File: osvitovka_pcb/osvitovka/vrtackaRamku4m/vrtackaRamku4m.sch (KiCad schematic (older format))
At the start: 21 parts, among them J1 Screw_Terminal_01x01, J2 Screw_Terminal_01x01, J3 M+, J4 M-, K1 RSM822, Q1 BC817, U1 LM78M05_TO220

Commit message: test a upgrade pcb.
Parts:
- D1, D2: footprint Diode_SMD:D_1206_3216Metric -> Diode_SMD:D_1806_4516Metric_Pad1.57x1.80mm_HandSolder
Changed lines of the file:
@@
 F 0 "D2" V 6554 3279 50  0000 L CNN
 F 1 "D" V 6645 3279 50  0000 L CNN
-F 2 "Diode_SMD:D_1206_3216Metric" H 6600 3200 50  0001 C CNN
+F 2 "Diode_SMD:D_1806_4516Metric_Pad1.57x1.80mm_HandSolder" H 6600 3200 50  0001 C CNN
 F 3 "~" H 6600 3200 50  0001 C CNN
 	1    6600 3200
@@
 F 0 "D1" H 5300 2666 50  0000 C CNN
 F 1 "D" H 5300 2575 50  0000 C CNN
-F 2 "Diode_SMD:D_1206_3216Metric" H 5300 2450 50  0001 C CNN
+F 2 "Diode_SMD:D_1806_4516Metric_Pad1.57x1.80mm_HandSolder" H 5300 2450 50  0001 C CNN
 F 3 "~" H 5300 2450 50  0001 C CNN
 	1    5300 2450

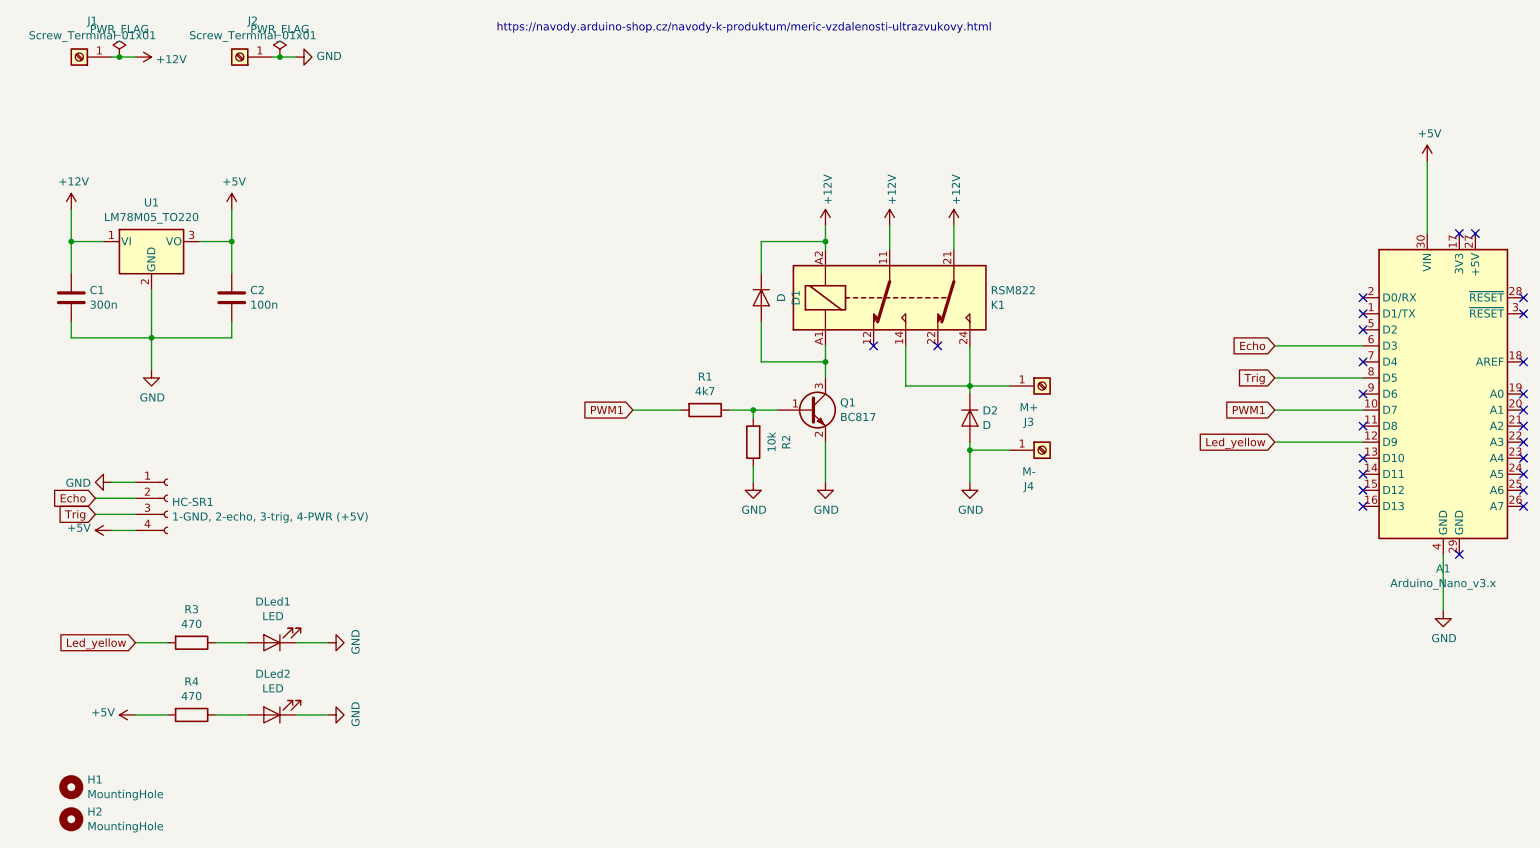
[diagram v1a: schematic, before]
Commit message: Totálně předělaný plošňák. Zvětšené plošky, širší cestičky. Založena vlastní knihovna.
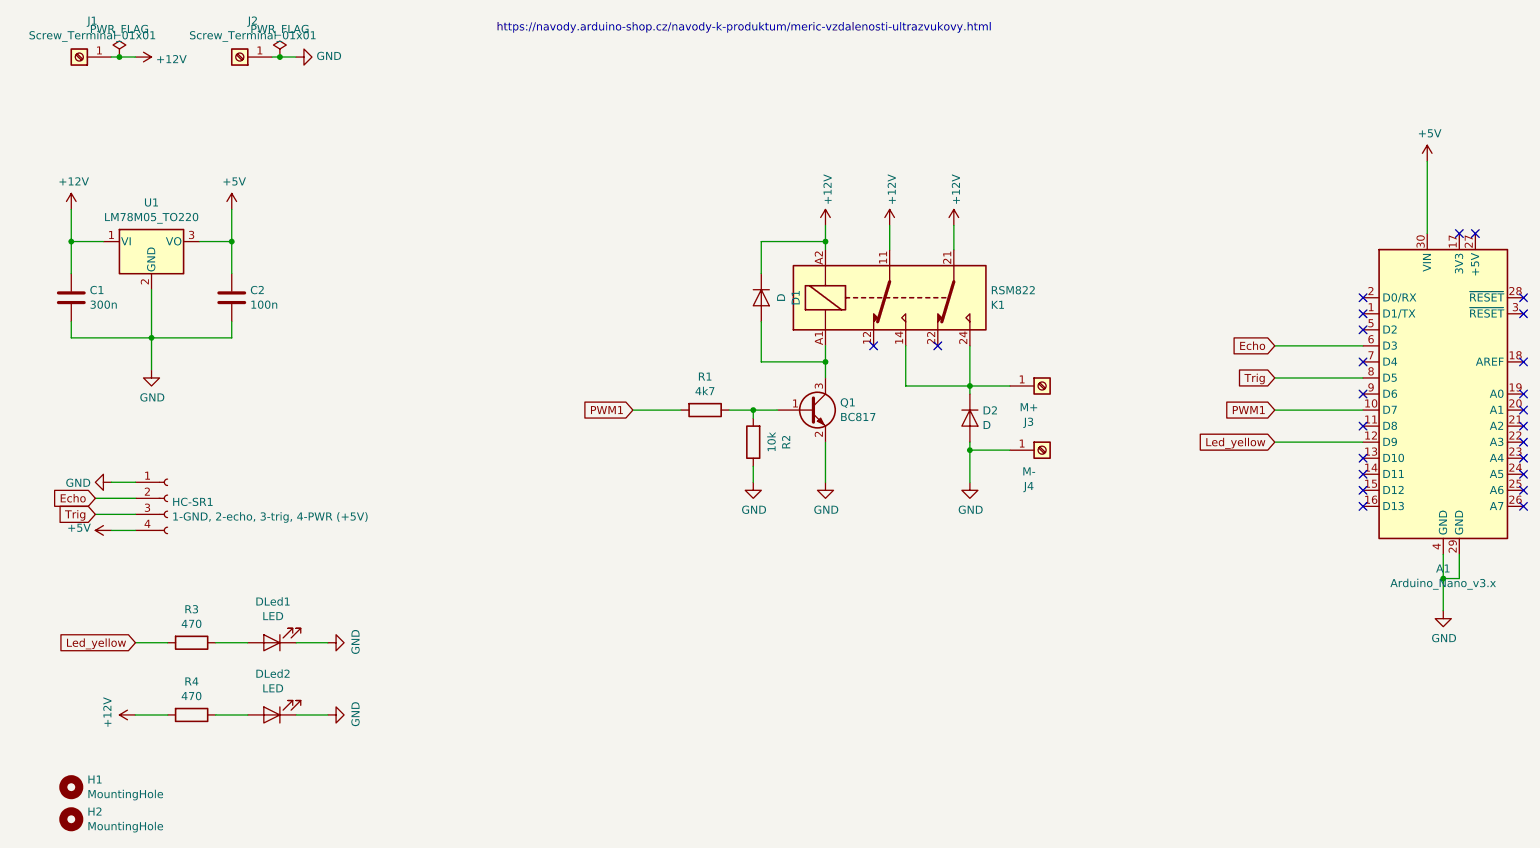
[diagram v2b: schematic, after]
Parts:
- A1: footprint Module:Arduino_Nano -> LPouzdra:Arduino_Nano_vetsi_plosky
- C1, C2: footprint Capacitor_THT:C_Disc_D3.0mm_W2.0mm_P2.50mm -> LPouzdra:AR_C_Disc_D3.0mm_W2.0mm_P2.50mm
- D1, D2: footprint Diode_SMD:D_1806_4516Metric_Pad1.57x1.80mm_HandSolder -> Diode_SMD:D_2010_5025Metric_Pad1.52x2.65mm_HandSolder
- DLed1, DLed2: footprint LED_THT:LED_D3.0mm -> LPouzdra:AR_LED_D3.0mm
- HC-SR1: footprint Connector_PinHeader_2.54mm:PinHeader_1x04_P2.54mm_Vertical -> LPouzdra:AR_PinHeader_1x04_P2.54mm_Vertical
- K1: footprint Relay_THT:Relay_DPDT_Finder_30.22 -> LPouzdra:AR_Relay_DPDT_Finder_30.22
- U1: footprint Package_TO_SOT_THT:TO-220-3_Vertical -> LPouzdra:AR_TO-220-3_Vertical
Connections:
- net +12V: now also R4.2
- net +5V: no longer R4.2
- net GND: now also A1.29 (GND)
- no-connect marks 26 -> 25
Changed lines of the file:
@@
 F 0 "C1" H 1115 2496 50  0000 L CNN
 F 1 "300n" H 1115 2405 50  0000 L CNN
-F 2 "Capacitor_THT:C_Disc_D3.0mm_W2.0mm_P2.50mm" H 1038 2300 50  0001 C CNN
+F 2 "LPouzdra:AR_C_Disc_D3.0mm_W2.0mm_P2.50mm" H 1038 2300 50  0001 C CNN
 F 3 "~" H 1000 2450 50  0001 C CNN
 	1    1000 2450
@@
 F 0 "U1" H 1500 2342 50  0000 C CNN
 F 1 "LM78M05_TO220" H 1500 2251 50  0000 C CNN
-F 2 "Package_TO_SOT_THT:TO-220-3_Vertical" H 1500 2325 50  0001 C CIN
+F 2 "LPouzdra:AR_TO-220-3_Vertical" H 1500 2325 50  0001 C CIN
 F 3 "http://www.fairchildsemi.com/ds/LM/LM78M05.pdf" H 1500 2050 50  0001 C CNN
 	1    1500 2100
@@
 F 0 "C2" H 2115 2496 50  0000 L CNN
 F 1 "100n" H 2115 2405 50  0000 L CNN
-F 2 "Capacitor_THT:C_Disc_D3.0mm_W2.0mm_P2.50mm" H 2038 2300 50  0001 C CNN
+F 2 "LPouzdra:AR_C_Disc_D3.0mm_W2.0mm_P2.50mm" H 2038 2300 50  0001 C CNN
 F 3 "~" H 2000 2450 50  0001 C CNN
 	1    2000 2450
@@
 F 0 "HC-SR1" H 1628 3676 50  0000 L CNN
 F 1 "1-GND, 2-echo, 3-trig, 4-PWR (+5V)" H 1628 3585 50  0000 L CNN
-F 2 "Connector_PinHeader_2.54mm:PinHeader_1x04_P2.54mm_Vertical" H 1600 3700 50  0001 C CNN
+F 2 "LPouzdra:AR_PinHeader_1x04_P2.54mm_Vertical" H 1600 3700 50  0001 C CNN
 F 3 "~" H 1600 3700 50  0001 C CNN
 	1    1600 3700
@@
 F 0 "DLed1" H 2243 4345 50  0000 C CNN
 F 1 "LED" H 2243 4436 50  0000 C CNN
-F 2 "LED_THT:LED_D3.0mm" H 2250 4600 50  0001 C CNN
+F 2 "LPouzdra:AR_LED_D3.0mm" H 2250 4600 50  0001 C CNN
 F 3 "~" H 2250 4600 50  0001 C CNN
 	1    2250 4600
@@
 F 0 "DLed2" H 2243 4795 50  0000 C CNN
 F 1 "LED" H 2243 4886 50  0000 C CNN
-F 2 "LED_THT:LED_D3.0mm" H 2250 5050 50  0001 C CNN
+F 2 "LPouzdra:AR_LED_D3.0mm" H 2250 5050 50  0001 C CNN
 F 3 "~" H 2250 5050 50  0001 C CNN
 	1    2250 5050
@@
 F 0 "A1" H 9550 1961 50  0000 C CNN
 F 1 "Arduino_Nano_v3.x" H 9550 1870 50  0000 C CNN
-F 2 "Module:Arduino_Nano" H 9550 3050 50  0001 C CIN
+F 2 "LPouzdra:Arduino_Nano_vetsi_plosky" H 9550 3050 50  0001 C CIN
 F 3 "http://www.mouser.com/pdfdocs/Gravitech_Arduino_Nano3_0.pdf" H 9550 3050 50  0001 C CNN
 	1    9550 3050
@@
 	8500 3350 9050 3350
 Wire Wire Line
-	9550 4050 9550 4400
+	9550 4050 9550 4200
 Wire Wire Line
 	9450 1600 9450 2050
@@
 	8500 2950 9050 2950
 NoConn ~ 9050 2850
-NoConn ~ 9650 4050
 Wire Wire Line
 	8500 3150 9050 3150
@@
 F 0 "K1" H 6730 2496 50  0000 L CNN
 F 1 "RSM822" H 6730 2405 50  0000 L CNN
-F 2 "Relay_THT:Relay_DPDT_Finder_30.22" H 7450 2420 50  0001 C CNN
+F 2 "LPouzdra:AR_Relay_DPDT_Finder_30.22" H 7450 2420 50  0001 C CNN
 F 3 "http://www.relpol.pl/en/content/download/14975/202519/file/e_RSM822.pdf" H 6100 2450 50  0001 C CNN
 	1    6100 2450
@@
 F 0 "D2" V 6554 3279 50  0000 L CNN
 F 1 "D" V 6645 3279 50  0000 L CNN
-F 2 "Diode_SMD:D_1806_4516Metric_Pad1.57x1.80mm_HandSolder" H 6600 3200 50  0001 C CNN
+F 2 "Diode_SMD:D_2010_5025Metric_Pad1.52x2.65mm_HandSolder" H 6600 3200 50  0001 C CNN
 F 3 "~" H 6600 3200 50  0001 C CNN
 	1    6600 3200
@@
 F 0 "D1" H 5300 2666 50  0000 C CNN
 F 1 "D" H 5300 2575 50  0000 C CNN
-F 2 "Diode_SMD:D_1806_4516Metric_Pad1.57x1.80mm_HandSolder" H 5300 2450 50  0001 C CNN
+F 2 "Diode_SMD:D_2010_5025Metric_Pad1.52x2.65mm_HandSolder" H 5300 2450 50  0001 C CNN
 F 3 "~" H 5300 2450 50  0001 C CNN
 	1    5300 2450
@@
 Wire Wire Line
 	6600 3050 6600 3000
-$Comp
-L power:+5V #PWR0101
-U 1 1 5FDA6872
+NoConn ~ 9050 3450
+$Comp
+L power:+12V #PWR0101
+U 1 1 5FE1526E
 P 1400 5050
 F 0 "#PWR0101" H 1400 4900 50  0001 C CNN
-F 1 "+5V" V 1415 5178 50  0000 L CNN
+F 1 "+12V" H 1415 5223 50  0000 C CNN
 F 2 "" H 1400 5050 50  0001 C CNN
 F 3 "" H 1400 5050 50  0001 C CNN
@@
 	0    -1   -1   0
 $EndComp
-NoConn ~ 9050 3450
+Wire Wire Line
+	9650 4050 9650 4200
+Wire Wire Line
+	9650 4200 9550 4200
+Connection ~ 9550 4200
+Wire Wire Line
+	9550 4200 9550 4400
 $EndSCHEMATC
